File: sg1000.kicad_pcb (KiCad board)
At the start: 2 copper layers, 150 x 134.8 mm, 71 parts, among them CN1 Conn_01x07_Female, J1 USB-B1HSB6, J2 RCJ-014, J3 RCJ-013, Q1 2n4401, Q1c1 2n3906, SW1 Pause Key, SW2 Power Toggle, U1 SG-1000-Cart, U10 PLCCZ80, U100 74HCT574, U101 74HCT574, U102 74HCT574, U103 AS6C62256-DIP, U11 AS6C62256-DIP, U12 TMS9918A, U13 74LS139, U16 74LS32, U18 74LS257, U21 74LS257, U3 SN76489AN, U99 74HCT04, X2 10.73863MHz

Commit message: v0.2 begins
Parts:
- moved D2 25.8 mm to (67.3, 173.1), turned to 0 degrees
- moved R2 22.3 mm to (62.7, 173.1)
- moved SW2 0.79 mm to (30.7, 173.0)
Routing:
- net GND: track 229.8 -> 217.3 mm
- net +5V: track 412.2 -> 406.0 mm
- net Net-(D2-Pad1): track 6.00 -> 3.58 mm
- net /Fused_Power: track 18.8 -> 18.0 mm
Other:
- board text added: "CONTROLLER 1"
- board text added: "CONTROLLER 2"
- board text added: "PAUSE"
- board text added: "POWER"
- board text added: "v0.2"
- board text removed: "v0.1"
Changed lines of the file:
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@@
     (pad_to_mask_clearance 0.051)
     (solder_mask_min_width 0.25)
+    (grid_origin 146.685 179.07)
     (pcbplotparams
       (layerselection 0x00010fc_ffffffff)
@@
     (property "Sheetname" "")
     (attr through_hole)
-    (fp_text reference "SW1" (at 3.25 -2) (layer "F.SilkS")
+    (fp_text reference "SW1" (at -2.413 4.699 90) (layer "F.SilkS")
       (effects (font (size 1 1) (thickness 0.15)))
     )
@@
   )
   (footprint "LED_THT:LED_D3.0mm" (layer "F.Cu")
-    (at 41.656 175.768 180)
+    (at 67.305 173.101)
     (descr "LED, diameter 3.0mm, 2 pins")
     (tags "LED diameter 3.0mm 2 pins")
@@
     (fp_arc (start -0.23 -1.16619) (mid 3.17 0.000452) (end -0.230555 1.165476) (layer "F.Fab") (width 0.1))
     (fp_circle (center 1.27 0) (end 2.77 0) (layer "F.Fab") (width 0.1) (fill none))
-    (pad "1" thru_hole rect (at 0 0 180) (size 1.8 1.8) (drill 0.9) (layers *.Cu *.Mask)
+    (pad "1" thru_hole rect (at 0 0) (size 1.8 1.8) (drill 0.9) (layers *.Cu *.Mask)
       (net 136 "Net-(D2-Pad1)") (pinfunction "K") (pintype "passive"))
-    (pad "2" thru_hole circle (at 2.54 0 180) (size 1.8 1.8) (drill 0.9) (layers *.Cu *.Mask)
+    (pad "2" thru_hole circle (at 2.54 0) (size 1.8 1.8) (drill 0.9) (layers *.Cu *.Mask)
       (net 2 "+5V") (pinfunction "A") (pintype "passive"))
     (model "${KICAD6_3DMODEL_DIR}/LED_THT.3dshapes/LED_D3.0mm.wrl"
@@
   )
   (footprint "Resistor_SMD:R_0805_2012Metric_Pad1.20x1.40mm_HandSolder" (layer "F.Cu")
-    (at 40.656 169.768 180)
+    (at 62.722 173.101 180)
     (descr "Resistor SMD 0805 (2012 Metric), square (rectangular) end terminal, IPC_7351 nominal with elongated pad for handsoldering. (Body size source: IPC-SM-782 page 72, https://www.pcb-3d.com/wordpress/wp-content/uploads/ipc-sm-782a_amendment_1_and_2.pdf), generated with kicad-footprint-generator")
     (tags "resistor handsolder")
@@
   )
   (footprint "LeakyChips:PVA1_Switch" (layer "F.Cu")
-    (at 30.656 173.768)
+    (at 30.656 172.974)
     (descr "C&K PVA1 toggle switch")
     (property "Sheetfile" "sg1000.kicad_sch")
     (property "Sheetname" "")
     (attr through_hole)
-    (fp_text reference "SW2" (at 0 5.7) (layer "F.SilkS")
+    (fp_text reference "SW2" (at 5.666 -3.588 90) (layer "F.SilkS")
       (effects (font (size 1 1) (thickness 0.15)))
     )
@@
     (effects (font (size 1 1) (thickness 0.15)) (justify mirror))
   )
+  (gr_text "POWER" (at 30.607 179.451) (layer "F.SilkS")
+    (effects (font (size 1.5 1.5) (thickness 0.375)))
+  )
+  (gr_text "CONTROLLER 2" (at 141.605 163.83 90) (layer "F.SilkS")
+    (effects (font (size 1.5 1.5) (thickness 0.375)) (justify right))
+  )
   (gr_text "Enable A15 to cart" (at 161.925 82.423 90) (layer "F.SilkS")
     (effects (font (size 1 1) (thickness 0.15)))
@@
     (effects (font (size 1 1) (thickness 0.15)))
   )
-  (gr_text "v0.1" (at 96.774 137.668) (layer "F.SilkS")
+  (gr_text "v0.2" (at 96.774 137.668) (layer "F.SilkS")
     (effects (font (size 1 1) (thickness 0.15)))
   )
@@
     (effects (font (size 1 1) (thickness 0.15)))
   )
+  (gr_text "PAUSE" (at 152.273 179.07) (layer "F.SilkS")
+    (effects (font (size 1.5 1.5) (thickness 0.375)) (justify right))
+  )
   (gr_text "Audio" (at 51.943 48.895 90) (layer "F.SilkS")
     (effects (font (size 1 1) (thickness 0.15)))
@@
     (effects (font (size 1 1) (thickness 0.15)))
   )
+  (gr_text "CONTROLLER 1" (at 76.2 179.451) (layer "F.SilkS")
+    (effects (font (size 1.5 1.5) (thickness 0.375)) (justify right))
+  )
   (gr_text "Disable ~{CSCN4} pullup" (at 162.814 132.588 90) (layer "F.SilkS")
     (effects (font (size 1 1) (thickness 0.15)))
   )
   (segment (start 81.82 47.625) (end 79.915 49.53) (width 0.5) (layer "F.Cu") (net 1))
-  (segment (start 32.156 164.618) (end 37.156 169.618) (width 1) (layer "F.Cu") (net 1))
   (segment (start 76.32452 48.38048) (end 75.175 49.53) (width 0.5) (layer "F.Cu") (net 1))
   (segment (start 123.257 172.556001) (end 126.027002 172.556001) (width 1) (layer "F.Cu") (net 1))
@@
   (segment (start 97.244897 171.106103) (end 99.702 168.649) (width 1) (layer "F.Cu") (net 1))
   (segment (start 56.515 134.62) (end 63.119 134.62) (width 1) (layer "F.Cu") (net 1))
+  (segment (start 60.198 173.101) (end 59.944 172.847) (width 0.5) (layer "F.Cu") (net 1))
   (segment (start 94.4665 52.9375) (end 94.488 52.959) (width 1) (layer "F.Cu") (net 1))
-  (segment (start 32.156 163.118) (end 32.156 164.618) (width 1) (layer "F.Cu") (net 1))
   (segment (start 148.699 70.376) (end 148.665 70.41) (width 1) (layer "F.Cu") (net 1))
   (segment (start 99.702 168.649) (end 99.702 164.451115) (width 1) (layer "F.Cu") (net 1))
@@
   (segment (start 87.757 103.632) (end 90.943 103.632) (width 1) (layer "F.Cu") (net 1))
   (segment (start 85.725 47.625) (end 81.82 47.625) (width 0.5) (layer "F.Cu") (net 1))
-  (segment (start 148.665 70.41) (end 151.849 70.41) (width 1) (layer "F.Cu") (net 1))
   (segment (start 64.389 133.35) (end 64.389 128.594689) (width 1) (layer "F.Cu") (net 1))
   (segment (start 78.359 99.187) (end 80.137 99.187) (width 1) (layer "F.Cu") (net 1))
@@
   (segment (start 160.401 70.376) (end 148.699 70.376) (width 1) (layer "F.Cu") (net 1))
   (segment (start 48.387 119.056) (end 53.156 119.056) (width 1) (layer "F.Cu") (net 1))
-  (segment (start 151.849 70.41) (end 151.892 70.367) (width 1) (layer "F.Cu") (net 1))
   (segment (start 72.98352 98.00852) (end 72.98352 95.04752) (width 1) (layer "F.Cu") (net 1))
   (segment (start 93.640001 172.554914) (end 95.088812 171.106103) (width 1) (layer "F.Cu") (net 1))
@@
   (segment (start 133.347 154.916115) (end 134.226511 155.795626) (width 1) (layer "F.Cu") (net 1))
   (segment (start 75.885 100.91) (end 72.98352 98.00852) (width 1) (layer "F.Cu") (net 1))
+  (segment (start 61.722 173.101) (end 60.198 173.101) (width 0.5) (layer "F.Cu") (net 1))
   (segment (start 53.213 127.381) (end 53.213 131.318) (width 1) (layer "F.Cu") (net 1))
   (segment (start 22.097 68.2) (end 21.844 68.453) (width 1) (layer "F.Cu") (net 1))
   (segment (start 43.437 115.951) (end 48.387 115.951) (width 1) (layer "F.Cu") (net 1))
-  (segment (start 37.306 169.768) (end 37.156 169.618) (width 1) (layer "F.Cu") (net 1))
   (segment (start 43.18 161.036) (end 40.757 161.036) (width 1) (layer "F.Cu") (net 1))
-  (segment (start 39.656 169.768) (end 37.306 169.768) (width 1) (layer "F.Cu") (net 1))
   (via (at 80.137 99.187) (size 0.8) (drill 0.4) (layers "F.Cu" "B.Cu") (net 1))
   (via (at 53.213 127.381) (size 0.8) (drill 0.4) (layers "F.Cu" "B.Cu") (net 1))
   (via (at 101.727 103.632) (size 0.8) (drill 0.4) (layers "F.Cu" "B.Cu") (net 1))
-  (via (at 37.156 169.618) (size 0.8) (drill 0.4) (layers "F.Cu" "B.Cu") (net 1))
   (via (at 48.387 115.951) (size 0.8) (drill 0.4) (layers "F.Cu" "B.Cu") (net 1))
   (via (at 21.844 68.453) (size 0.8) (drill 0.4) (layers "F.Cu" "B.Cu") (net 1))
@@
   (via (at 94.488 52.959) (size 0.8) (drill 0.4) (layers "F.Cu" "B.Cu") (net 1))
   (via (at 88.646 99.441) (size 0.8) (drill 0.4) (layers "F.Cu" "B.Cu") (net 1))
+  (via (at 59.944 172.847) (size 0.8) (drill 0.4) (layers "F.Cu" "B.Cu") (net 1))
   (via (at 63.2835 127.568161) (size 0.8) (drill 0.4) (layers "F.Cu" "B.Cu") (net 1))
   (via (at 80.3015 109.040129) (size 0.8) (drill 0.4) (layers "F.Cu" "B.Cu") (net 1))
@@
   (segment (start 48.32 90.354) (end 46.101 88.135) (width 1) (layer "F.Cu") (net 2))
   (segment (start 61.087 70.231) (end 60.706 70.612) (width 1) (layer "F.Cu") (net 2))
-  (segment (start 33.196 176.562) (end 33.196 170.593) (width 1) (layer "F.Cu") (net 2))
-  (segment (start 33.196 176.562) (end 38.322 176.562) (width 1) (layer "F.Cu") (net 2))
+  (segment (start 33.196 169.799) (end 33.196 175.768) (width 1) (layer "F.Cu") (net 2))
   (segment (start 60.706 70.612) (end 51.054 70.612) (width 1) (layer "F.Cu") (net 2))
   (segment (start 77.074 146.573) (end 83.093885 146.573) (width 1) (layer "F.Cu") (net 2))
@@
   (segment (start 45.906 83.625) (end 40.68 83.625) (width 1) (layer "F.Cu") (net 2))
   (segment (start 75.946 113.03) (end 75.885 112.969) (width 1) (layer "F.Cu") (net 2))
-  (segment (start 38.322 176.562) (end 39.116 175.768) (width 1) (layer "F.Cu") (net 2))
   (segment (start 84.582 113.03) (end 75.946 113.03) (width 1) (layer "F.Cu") (net 2))
   (segment (start 75.885 112.969) (end 75.885 105.99) (width 1) (layer "F.Cu") (net 2))
@@
   (segment (start 160.167 130.83) (end 146.015 130.83) (width 0.25) (layer "F.Cu") (net 127))
   (segment (start 160.528 131.191) (end 160.167 130.83) (width 0.25) (layer "F.Cu") (net 127))
-  (segment (start 150.099 130.81) (end 150.079 130.83) (width 0.25) (layer "F.Cu") (net 127))
-  (segment (start 41.656 175.768) (end 41.656 169.768) (width 0.25) (layer "F.Cu") (net 136))
+  (segment (start 67.305 173.101) (end 63.722 173.101) (width 0.5) (layer "F.Cu") (net 136))
   (segment (start 28.116 170.593) (end 28.116 164.658) (width 1) (layer "F.Cu") (net 139))
   (segment (start 28.091 170.618) (end 28.116 170.593) (width 1) (layer "F.Cu") (net 139))
   (segment (start 28.116 164.658) (end 29.656 163.118) (width 1) (layer "F.Cu") (net 139))
   (segment (start 23.366 170.618) (end 28.091 170.618) (width 1) (layer "F.Cu") (net 139))
-  (segment (start 28.116 176.562) (end 28.116 170.593) (width 1) (layer "F.Cu") (net 139))
+  (segment (start 28.116 170.593) (end 28.116 175.768) (width 1) (layer "F.Cu") (net 139))
   (segment (start 22.25 61.21) (end 22.25 61.25) (width 1) (layer "F.Cu") (net 140))
   (segment (start 15.5 68) (end 22.25 61.25) (width 1) (layer "F.Cu") (net 140))

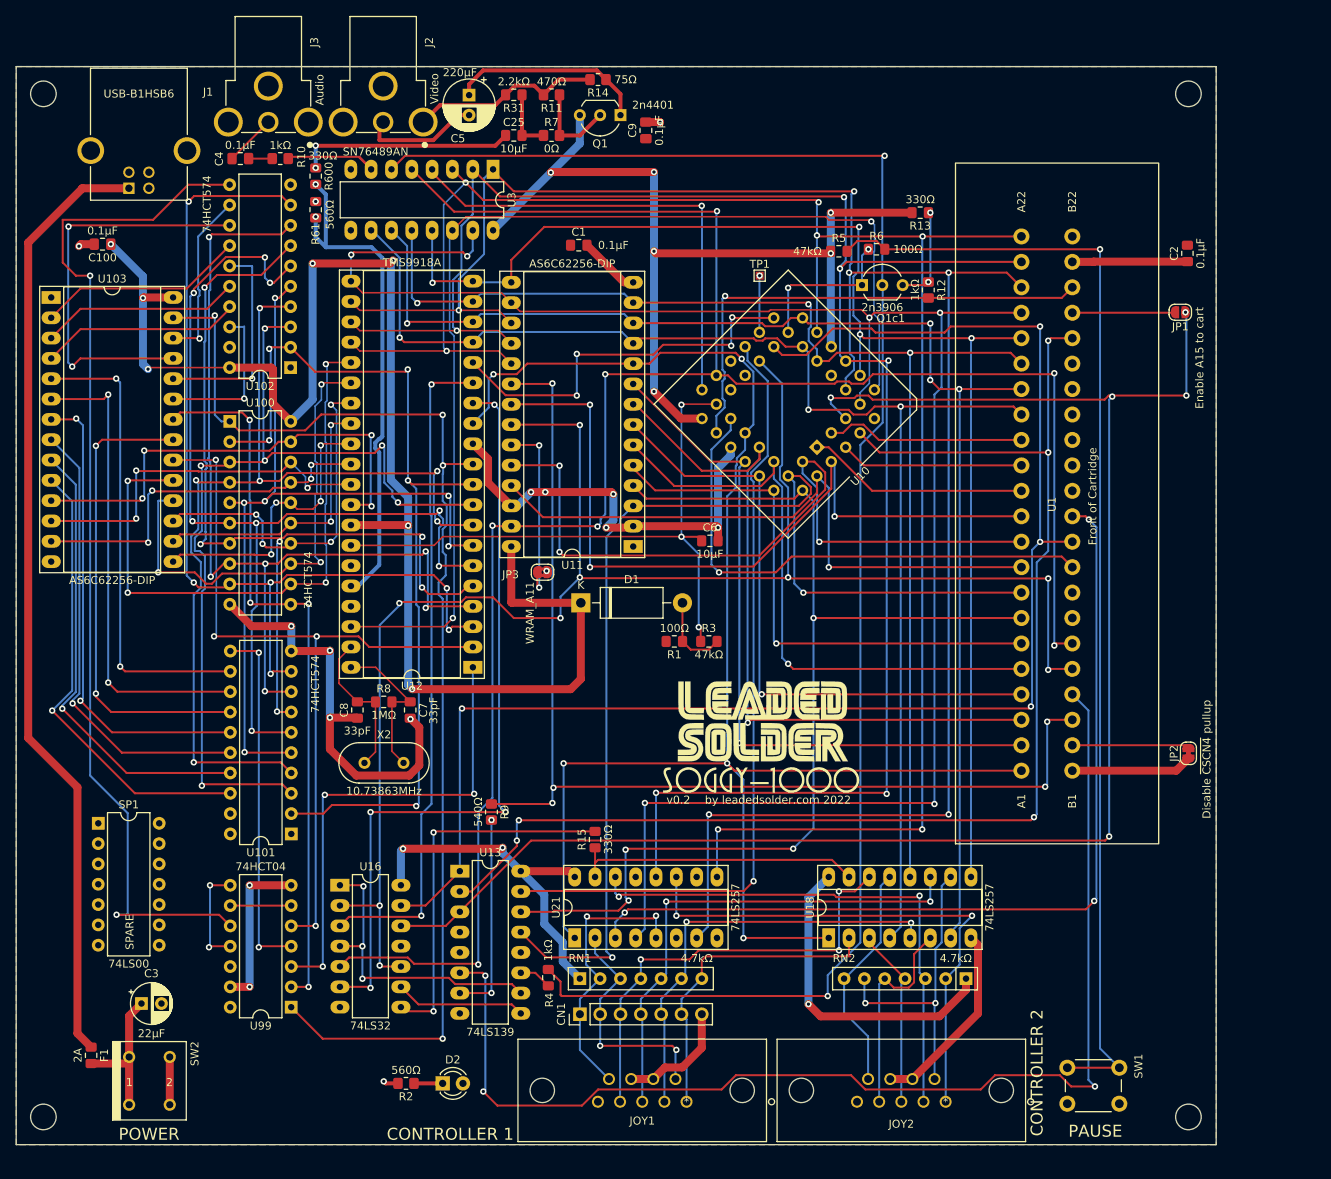
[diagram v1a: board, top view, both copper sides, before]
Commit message: Turn the controller ports around so you can use them
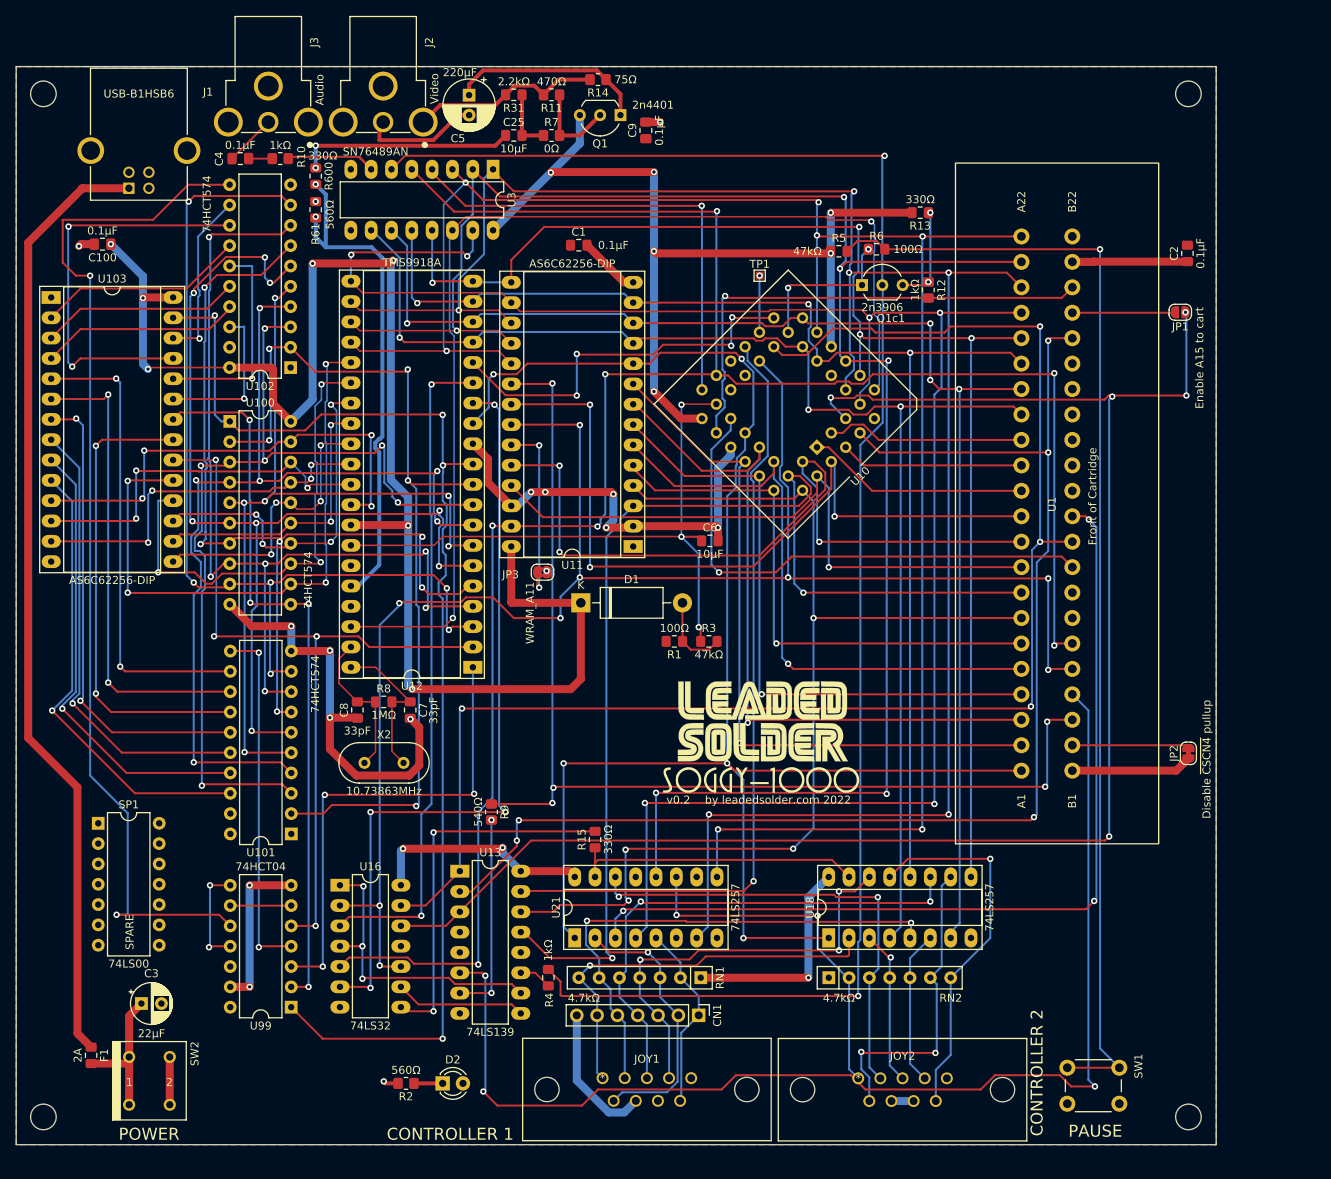
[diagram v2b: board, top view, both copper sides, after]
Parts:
- moved RN2 17.2 mm to (115.6, 159.9), turned to 0 degrees
- moved RN1 15.1 mm to (99.6, 159.9), turned to 180 degrees
- moved CN1 14.9 mm to (99.3, 164.6), turned to -90 degrees
- moved JOY2 11.3 mm to (119.3, 172.5), turned to 0 degrees
- moved JOY1 10.9 mm to (87.3, 172.4), turned to 0 degrees
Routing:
- net +5V: track 406.0 -> 376.5 mm
- net /JOY2_UP: track 66.4 -> 45.0 mm
- net GND: track 217.3 -> 199.0 mm
- net /JOY2_BUTTON2: track 28.9 -> 46.6 mm, vias 0 -> 1
- net /JOY1_BUTTON2: track 35.3 -> 23.5 mm, vias 2 -> 0
- net /JOY1_UP: track 39.9 -> 50.9 mm, vias 0 -> 1
- net /JOY1_DOWN: track 54.0 -> 64.3 mm
- net /JOY2_DOWN: track 66.7 -> 59.0 mm
- net /JOY2_RIGHT: track 26.5 -> 19.4 mm
- net /JOY1_BUTTON1: track 29.3 -> 34.1 mm, vias 2 -> 1
- net /JOY2_LEFT: track 22.5 -> 19.5 mm, vias 0 -> 1
- net /JOY1_RIGHT: track 56.0 -> 53.6 mm
- net /~{CS_PSG}: track 207.6 -> 209.9 mm
- net /JOY1_LEFT: track 62.5 -> 64.0 mm
- net /JOY2_BUTTON1: track 38.0 -> 39.3 mm
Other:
- board text added: "keyboard edge connector here?"

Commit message: Add edge connector
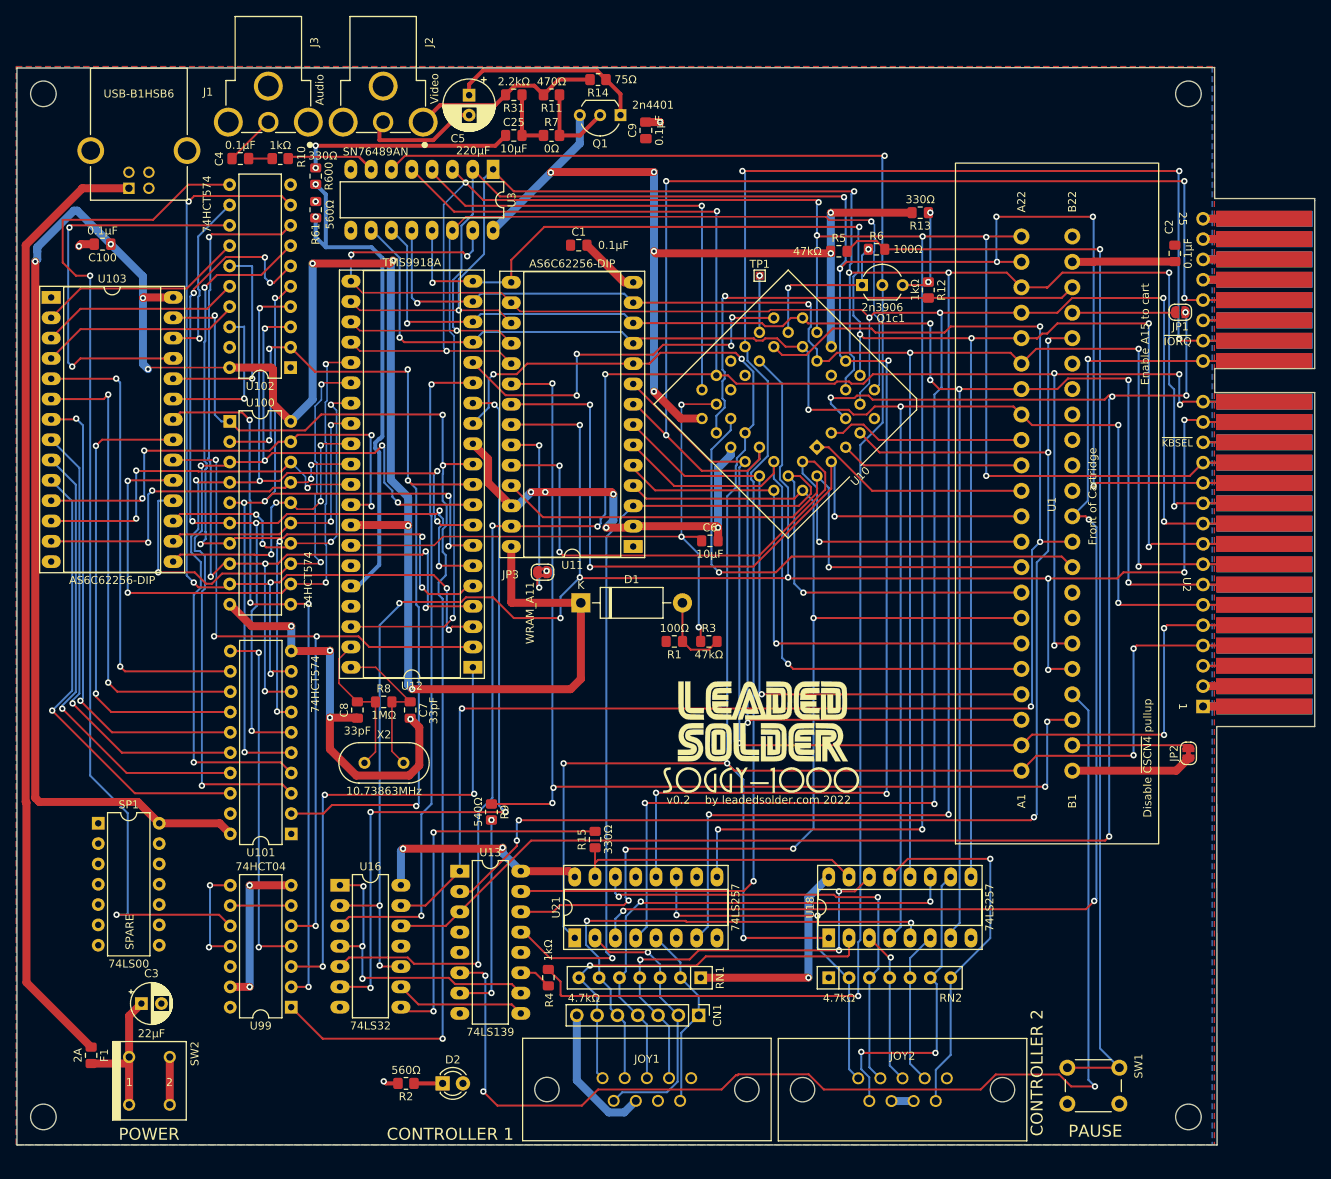
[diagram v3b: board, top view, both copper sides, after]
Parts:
- added U2: SG-1000-Expansion, LeadedSolder:SG1000_Edge, F.Cu at (159.8, 110.7)
- moved C2 1.57 mm to (158.8, 69.4)
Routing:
- net +5V: track 376.5 -> 515.2 mm, vias 16 -> 17
- net /A2: track 90.7 -> 219.6 mm, vias 1 -> 5
- net /~{IORQ}: track 97.8 -> 214.0 mm, vias 1 -> 4
- net /D6: track 233.6 -> 314.2 mm, vias 6 -> 10
- net /D7: track 238.6 -> 311.6 mm, vias 7 -> 9
- net /D5: track 248.7 -> 316.6 mm, vias 6 -> 8
- net /D3: track 171.5 -> 238.5 mm, vias 4 -> 6
- net /D4: track 234.7 -> 301.5 mm, vias 6 -> 8
- net /D2: track 159.2 -> 225.3 mm, vias 3 -> 5
- net /D1: track 167.7 -> 231.8 mm, vias 4 -> 6
- net /D0: track 170.5 -> 231.4 mm, vias 3 -> 5
- net GND: track 199.0 -> 258.8 mm
- net /~{RD}: track 211.2 -> 265.3 mm, vias 9 -> 11
- net /A0: track 205.6 -> 257.9 mm, vias 5 -> 7
- net /A1: track 88.9 -> 140.9 mm, vias 1 -> 3
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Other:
- board size 150 x 134.8 mm -> 150 x 134.7 mm
- board text added: "~{IORQ}"
- board text added: "~{KBSEL}"
